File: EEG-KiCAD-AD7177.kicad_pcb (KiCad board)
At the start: 2 copper layers, 35.6 x 21.7 mm, 53 parts, among them J1 IN EEG, J2 Battery, J3 Programmer, J4 Vs+ Ele, J5 Vs- Ele, U1 AD7177-2, U2 OPA2210, U3 NRF528XX-QFAA, U4 RP511Z331_3.3V, U5 XCL101A501-5V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

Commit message: With description
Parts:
- moved C6 0.21 mm to (201.2, 127.9)
- moved C7 0.19 mm to (201.5, 129.0)
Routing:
- net AGND: track 110.5 -> 113.5 mm
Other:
- board text added: "BIAS"
- board text added: "Batt+"
- board text added: "Batt-"
- board text added: "CLK"
- board text added: "IN0"
- board text added: "IN1"
- board text added: "IN2"
- board text added: "IN3"
- board text added: "IN4"
- board text added: "IO"
- board text added: "V+"
- board text added: "V-"

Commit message: Done
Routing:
- net /INBIAS: track 2.64 -> 13.6 mm, vias 0 -> 1
- net AGND: track 113.5 -> 116.0 mm
- net Net-(C16-Pad2): track 7.61 -> 7.62 mm, vias 0 -> 2
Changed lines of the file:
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@@
     (thickness 1.6)
     (drawings 25)
-    (tracks 524)
+    (tracks 547)
     (zones 0)
     (modules 53)
@@
   (layers
     (0 F.Cu signal)
-    (31 B.Cu signal hide)
+    (31 B.Cu signal)
     (32 B.Adhes user)
     (33 F.Adhes user)
@@
   (segment (start 197.29 139.56) (end 197.29 138.415) (width 0.1524) (layer F.Cu) (net 17))
   (segment (start 198.34 137.365) (end 198.13 137.575) (width 0.1524) (layer F.Cu) (net 17))
-  (segment (start 198.79 132.9) (end 198.79 133.695) (width 0.1524) (layer F.Cu) (net 17))
   (segment (start 196.698614 131.033886) (end 196.254864 130.590136) (width 0.1524) (layer F.Cu) (net 17))
   (segment (start 196.698614 131.921386) (end 196.698614 131.033886) (width 0.1524) (layer F.Cu) (net 17))
@@
   (segment (start 198.698614 130.721386) (end 199.559208 130.721386) (width 0.1524) (layer F.Cu) (net 12))
   (segment (start 199.559208 130.721386) (end 200.62 131.782178) (width 0.1524) (layer F.Cu) (net 12))
-  (segment (start 193.18958 133.42967) (end 193.18958 133.53) (width 0.1524) (layer F.Cu) (net 17))
   (segment (start 193.58 133.53) (end 193.95 133.16) (width 0.1524) (layer F.Cu) (net 17))
   (segment (start 193.18958 133.53) (end 193.58 133.53) (width 0.1524) (layer F.Cu) (net 17))
@@
   (segment (start 201.5719 127.01) (end 202.8729 128.311) (width 0.1524) (layer F.Cu) (net 17))
   (segment (start 200.95 127.01) (end 201.5719 127.01) (width 0.1524) (layer F.Cu) (net 17))
+  (segment (start 193.18958 133.42967) (end 193.18958 133.53) (width 0.1524) (layer F.Cu) (net 17))
+  (segment (start 192.84 132.81) (end 193.18958 133.53) (width 0.1524) (layer F.Cu) (net 17))
+  (segment (start 191.248944 133.570966) (end 191.78 133.03991) (width 0.1524) (layer F.Cu) (net 17))
+  (segment (start 191.148614 133.570966) (end 191.248944 133.570966) (width 0.1524) (layer F.Cu) (net 17))
+  (segment (start 191.78 133.03991) (end 191.78 132.71) (width 0.1524) (layer F.Cu) (net 17))
+  (segment (start 191.78 132.71) (end 192 132.49) (width 0.1524) (layer F.Cu) (net 17))
+  (segment (start 192 132.49) (end 192.52 132.49) (width 0.1524) (layer F.Cu) (net 17))
+  (segment (start 192.52 132.49) (end 192.84 132.81) (width 0.1524) (layer F.Cu) (net 17))
   (via (at 192.827775 131.530225) (size 0.508) (drill 0.3302) (layers F.Cu B.Cu) (net 18))
   (segment (start 192.698614 131.121386) (end 192.698614 131.401064) (width 0.229) (layer F.Cu) (net 18))
@@
   (segment (start 207.37 137.1) (end 207.36 137.11) (width 0.1524) (layer F.Cu) (net 23))
   (segment (start 207.37 136.04) (end 207.37 137.1) (width 0.1524) (layer F.Cu) (net 23))
-  (segment (start 207.76 135) (end 207.365 135) (width 0.1524) (layer F.Cu) (net 23))
-  (segment (start 208.71 135) (end 207.76 135) (width 0.1524) (layer F.Cu) (net 23))
-  (segment (start 209.5 134.21) (end 208.71 135) (width 0.1524) (layer F.Cu) (net 23))
-  (segment (start 209.5 133.79) (end 209.5 134.21) (width 0.1524) (layer F.Cu) (net 23))
   (segment (start 212.363388 137.801612) (end 212.825 137.34) (width 0.1524) (layer F.Cu) (net 23))
   (segment (start 212.09599 138.06901) (end 212.363388 137.801612) (width 0.1524) (layer F.Cu) (net 23))
@@
   (segment (start 209.19 135.995) (end 209.80599 136.61099) (width 0.1524) (layer F.Cu) (net 23))
   (segment (start 208.77 135.995) (end 209.19 135.995) (width 0.1524) (layer F.Cu) (net 23))
+  (segment (start 207.76 135) (end 207.365 135) (width 0.1524) (layer F.Cu) (net 23))
+  (segment (start 208.54 134.51) (end 207.76 135) (width 0.1524) (layer F.Cu) (net 23))
+  (segment (start 209.5 133.79) (end 208.91 134.394375) (width 0.1524) (layer F.Cu) (net 23))
+  (segment (start 208.91 134.394375) (end 208.54 134.51) (width 0.1524) (layer F.Cu) (net 23))
   (segment (start 209.19 136.965) (end 208.77 136.965) (width 0.1524) (layer F.Cu) (net 24))
   (segment (start 210.3375 136.965) (end 209.19 136.965) (width 0.1524) (layer F.Cu) (net 24))
   (segment (start 210.7125 137.34) (end 210.3375 136.965) (width 0.1524) (layer F.Cu) (net 24))
   (segment (start 211.25 137.34) (end 210.7125 137.34) (width 0.1524) (layer F.Cu) (net 24))
+  (segment (start 208.435832 136.630832) (end 208.77 136.965) (width 0.1524) (layer F.Cu) (net 24))
+  (segment (start 208.22139 136.41639) (end 208.435832 136.630832) (width 0.1524) (layer F.Cu) (net 24))
+  (segment (start 208.22139 135.51861) (end 208.22139 136.41639) (width 0.1524) (layer F.Cu) (net 24))
+  (segment (start 209.40139 134.33861) (end 208.22139 135.51861) (width 0.1524) (layer F.Cu) (net 24))
+  (segment (start 209.80329 134.33861) (end 209.40139 134.33861) (width 0.1524) (layer F.Cu) (net 24))
+  (segment (start 210.0819 134.06) (end 209.80329 134.33861) (width 0.1524) (layer F.Cu) (net 24))
+  (segment (start 210.95 134.06) (end 210.0819 134.06) (width 0.1524) (layer F.Cu) (net 24))
+  (via (at 211.97 137.32) (size 0.508) (drill 0.3302) (layers F.Cu B.Cu) (net 24))
+  (segment (start 211.25 137.34) (end 211.95 137.34) (width 0.1524) (layer F.Cu) (net 24))
+  (segment (start 211.95 137.34) (end 211.97 137.32) (width 0.1524) (layer F.Cu) (net 24))
+  (segment (start 213.62 137.32) (end 216.18 139.88) (width 0.1524) (layer B.Cu) (net 24))
+  (segment (start 211.97 137.32) (end 213.62 137.32) (width 0.1524) (layer B.Cu) (net 24))
   (segment (start 192.29042 133.63033) (end 192.29042 133.53) (width 0.1524) (layer F.Cu) (net 25))
   (segment (start 192.718411 134.058321) (end 192.29042 133.63033) (width 0.1524) (layer F.Cu) (net 25))
@@
   (segment (start 194.88 134.66) (end 194.2776 134.66) (width 0.1524) (layer F.Cu) (net 25))
   (segment (start 194.2776 134.66) (end 193.81 134.07) (width 0.1524) (layer F.Cu) (net 25))
-  (segment (start 192.29042 133.07788) (end 192.29042 133.53) (width 0.1524) (layer F.Cu) (net 25))
-  (segment (start 191.717603 132.505063) (end 192.29042 133.07788) (width 0.1524) (layer F.Cu) (net 25))
-  (segment (start 191.717603 130.618582) (end 191.717603 132.505063) (width 0.1524) (layer F.Cu) (net 25))
   (segment (start 192.014799 130.321386) (end 191.717603 130.618582) (width 0.1524) (layer F.Cu) (net 25))
   (segment (start 192.698614 130.321386) (end 192.014799 130.321386) (width 0.1524) (layer F.Cu) (net 25))
+  (via (at 192.3 132.9726) (size 0.508) (drill 0.3302) (layers F.Cu B.Cu) (net 25))
+  (segment (start 192.29042 133.53) (end 192.29042 132.98218) (width 0.1524) (layer F.Cu) (net 25))
+  (segment (start 192.29042 132.98218) (end 192.3 132.9726) (width 0.1524) (layer F.Cu) (net 25))
+  (via (at 191.74 132.051125) (size 0.508) (drill 0.3302) (layers F.Cu B.Cu) (net 25))
+  (segment (start 191.717603 130.618582) (end 191.717603 132.028728) (width 0.1524) (layer F.Cu) (net 25))
+  (segment (start 191.717603 132.028728) (end 191.74 132.051125) (width 0.1524) (layer F.Cu) (net 25))
+  (segment (start 191.74 132.4126) (end 192.3 132.9726) (width 0.1524) (layer B.Cu) (net 25))
+  (segment (start 191.74 132.051125) (end 191.74 132.4126) (width 0.1524) (layer B.Cu) (net 25))
   (segment (start 203.48 139.78) (end 203.49 139.79) (width 0.152) (layer F.Cu) (net 29))
   (segment (start 198.655 139.56) (end 198.26 139.56) (width 0.1524) (layer F.Cu) (net 27))

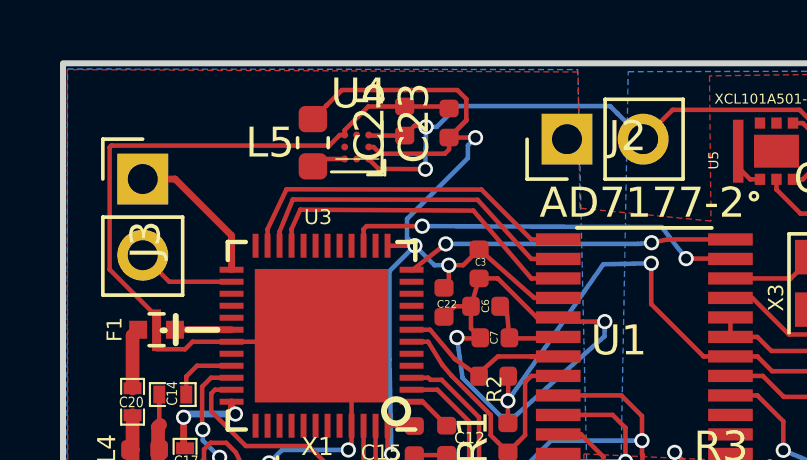
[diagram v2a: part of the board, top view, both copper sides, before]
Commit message: Fixed pins
Fixed wrong pins
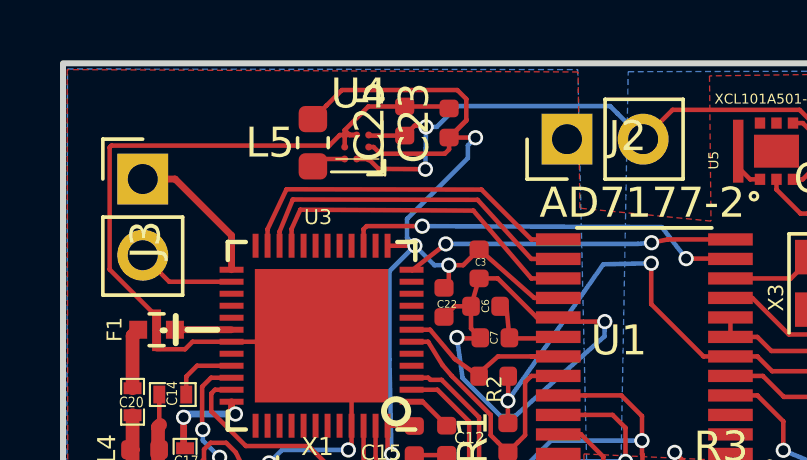
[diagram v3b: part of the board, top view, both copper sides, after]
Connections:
- U4 pad B1: Net-(U4-PadB1) -> Battery_Vin
- U4 pad B3: Net-(U4-PadB3) -> AGND
- U4 pad C2: Net-(U4-PadC2) -> AGND
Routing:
- net AGND: track 116.0 -> 117.2 mm
